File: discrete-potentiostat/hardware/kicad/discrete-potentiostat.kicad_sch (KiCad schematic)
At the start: 54 parts, among them J1 ELECTRODES, J2 SWD, U1 BQ51050BRHLR, U2 MIC5205-3.3YM5, U3 MDBT42Q-1MV2, U4 OPA2391, U5 REF35102QDBVR

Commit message: Replace BQ51050B direct-charge with BQ51013B + MCP73832 two-stage charging
Resolves the coin-cell charging risk: TI states BQ5105xB does not regulate
well below ~200mA, unsuitable for a 40mAh LIR2032. New chain follows TI's
guidance (Qi receiver -> 5V rail -> dedicated low-current charger), using
hand-solderable packages instead of the WCSP-only BQ51003/BQ25100 combo:

- BQ51013BRHLR: Qi WPC v1.2 receiver, regulated 5V out, VQFN-20. Pin map
  is the verified BQ51050BRHL family symbol with the two differing pins
  confirmed against the datasheet (4 OUT, 10 EN1). EN1=EN2=GND enables
  wireless; ILIM RILIM=250/IMAX -> 2.52k = 100mA; NTC stays on TS/CTRL.
- MCP73832T-2ACI/OT (official KiCad symbol): 4.2V linear charger,
  ICHG=1000/RPROG=20mA (0.5C), ~1.5mA termination, open-drain STAT ->
  CHG_N with the existing 100k pullup to 3V3.

Schematic regenerated and re-verified: all 38 design nets match the
kicad-cli extracted netlist exactly. Docs (README/design/BOM/firmware
plan/kicad README) updated to the two-stage chain; BQ51003+BQ25100 noted
as the drop-in denser alternative.

Co-Authored-By: Claude Fable 5 <noreply@anthropic.com>
Claude-Session: https://claude.ai/code/session_01GUNJUwfGKqvkZFmTaLQRu3
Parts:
- removed U1: BQ51050BRHLR, Package_DFN_QFN:Texas_VQFN-RHL-20, symbol Battery_Management:BQ51050BRHL
- added C27: 4.7u 10V, Capacitor_SMD:C_0603_1608Metric, symbol Device:C
- added U1: BQ51013BRHLR, Package_DFN_QFN:Texas_VQFN-RHL-20, symbol pstat:BQ51013BRHL
- added U6: MCP73832T-2ACI/OT, Package_TO_SOT_SMD:SOT-23-5, symbol Battery_Management:MCP73832-2-OT
- C10: value 1u 10V -> 4.7u 10V; footprint Capacitor_SMD:C_0402_1005Metric -> Capacitor_SMD:C_0603_1608Metric
- R1: value 15.4k 1% -> 2.32k 1%
- R3: value 2.4k 1% -> 49.9k 1%
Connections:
- net +BATT: now also C27.1, U6.3 (V_{BAT}); no longer C10.1, C11.1
- net AC1: now also U1.2 (AC1)
- net AC2: now also U1.19 (AC2)
- net BOOT1: now also U1.3 (BOOT1)
- net BOOT2: now also U1.17 (BOOT2)
- net CHG_N: now also U6.1 (STAT)
- net CLAMP1: now also U1.5 (CLAMP1)
- net CLAMP2: now also U1.16 (CLAMP2)
- net COMM1: now also U1.6 (COMM1)
- net COMM2: now also U1.15 (COMM2)
- net FOD: now also U1.14 (FOD)
- net GND: now also C27.2, U1.1 (PGND), U1.10 (EN1), U1.11 (EN2), U1.20 (PGND), U1.21 (PGND), U1.9 (AD), U6.2 (V_{SS})
- net ILIM: now also U1.12 (ILIM)
- net RECT: now also U1.18 (RECT)
- net TS: now also U1.13 (TS/CTRL)
- net TERM renamed PROG
- net PROG: now also U6.5 (PROG)
- new net V5OUT: C10.1, C11.1, U1.4 (OUT), U6.4 (V_{DD})
- no-connect marks 28 -> 29
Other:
- note added: "DISCRETE POTENTIOSTAT - wireless-charged 3-electrode chronoamperometry E_cell = WE - RE = 1.024V - 0.512V = +0.512V fixed. I_WE = (V(ADC_P)-V(ADC_N))/RF DESIGN NOTES / VERIFY BEFORE LAYOUT 1. CHARGING: two-stage per TI guidance for small cells. BQ51013B = Qi receiver with regulated 5V (V5OUT), ILIM: RILIM = 250/IMAX = R1+R2 = 2.52k -> IMAX 100mA (HW limit 120mA). MCP73832-2 (4.2V) charges the LIR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"
- note added: "QI RECEIVER 5V (BQ51013B) + 20mA CHARGER (MCP73832)"
- note removed: "DISCRETE POTENTIOSTAT - wireless-charged 3-electrode chronoamperometry E_cell = WE - RE = 1.024V - 0.512V = +0.512V fixed. I_WE = (V(ADC_P)-V(ADC_N))/RF DESIGN NOTES / VERIFY BEFORE LAYOUT 1. CHARGE CURRENT: IBULK = 314/RILIM = 314/(R1+R2) = 314/15.6k = 20mA (LIR2032 0.5C). TI states BQ5105xB regulates best >=200mA; at 20mA expect loose regulation and wide termination spread (R3 2.4k = 10% term).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"
- note removed: "QI WIRELESS RECEIVER + CHARGER (BQ51050B)"

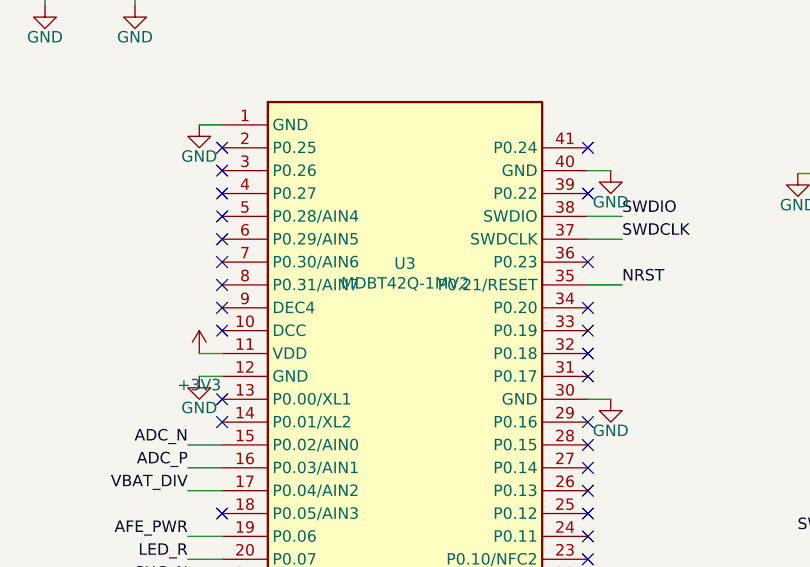
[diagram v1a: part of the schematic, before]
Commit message: Fix module part number: MDBT42Q-512KV2 (no 1MV2 variant exists for nRF52832)
Co-Authored-By: Claude Fable 5 <noreply@anthropic.com>
Claude-Session: https://claude.ai/code/session_01GUNJUwfGKqvkZFmTaLQRu3
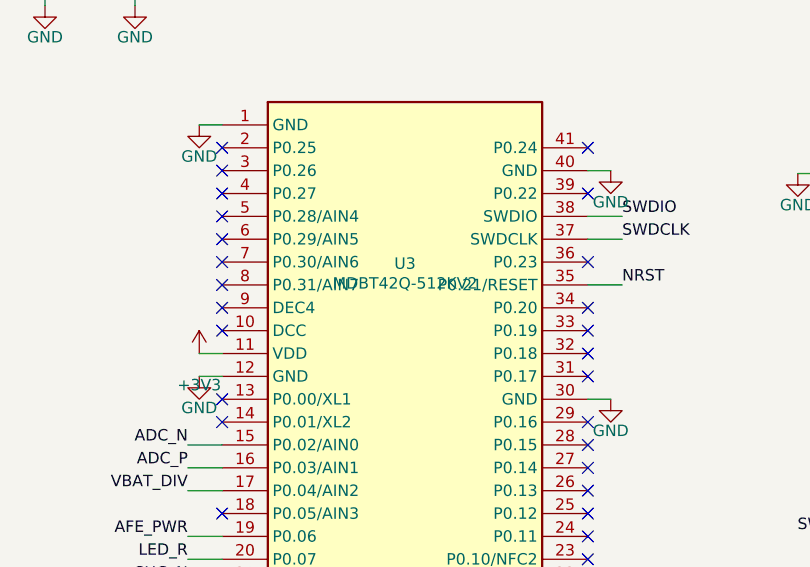
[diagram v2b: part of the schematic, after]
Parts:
- U3: value MDBT42Q-1MV2 -> MDBT42Q-512KV2

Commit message: Swap Qi coil to 760308101214 (19mm/26uH): smaller AND cheaper
The 26.3mm coil was a part-selection artifact, not a requirement — the
original sizing logic (device bounded by the battery) is restored. The
19mm WE-WPCC receiver coil costs less (~$7 vs ~$11), shrinks the PCB
from ~28mm to ~23mm disc, and our 0.13W charge load easily tolerates the
reduced coupling. Resonant caps retuned: C1 56n->100n, C2 560p->1n C0G.
Schematic regenerated, netlist re-verified (PASS); size/cost review
updated to the battery-bounded premise.

Co-Authored-By: Claude Fable 5 <noreply@anthropic.com>
Claude-Session: https://claude.ai/code/session_01GUNJUwfGKqvkZFmTaLQRu3
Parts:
- C1: value 56n C0G 50V -> 100n C0G 50V; footprint Capacitor_SMD:C_1206_3216Metric -> Capacitor_SMD:C_1210_3225Metric
- C2: value 560p C0G 50V -> 1n C0G 50V
- L1: value 760308101303 47uH -> 760308101214 26uH; footprint pstat:Wurth_760308101303 -> pstat:Wurth_760308101214

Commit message: Swap Qi coil to TDK WR202010-18M8-ID (20x20x1.0mm, 11uH, ~$3.6)
Cheapest verified candidate (half the 19mm Wurth) with the same footprint
class as the battery. Square outline: 22x22mm rounded-square puck instead
of a round disc (20x20 diagonal is 28.3mm). Resonant caps retuned for
11uH: C1 220nF C0G (fs 102kHz), C2 2.2nF C0G (fd ~1MHz). Schematic
regenerated, netlist verified (PASS).

Co-Authored-By: Claude Fable 5 <noreply@anthropic.com>
Claude-Session: https://claude.ai/code/session_01GUNJUwfGKqvkZFmTaLQRu3
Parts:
- C1: value 100n C0G 50V -> 220n C0G 50V
- C2: value 1n C0G 50V -> 2.2n C0G 50V
- L1: value 760308101214 26uH -> WR202010-18M8-ID 11uH; footprint pstat:Wurth_760308101214 -> pstat:TDK_WR202010

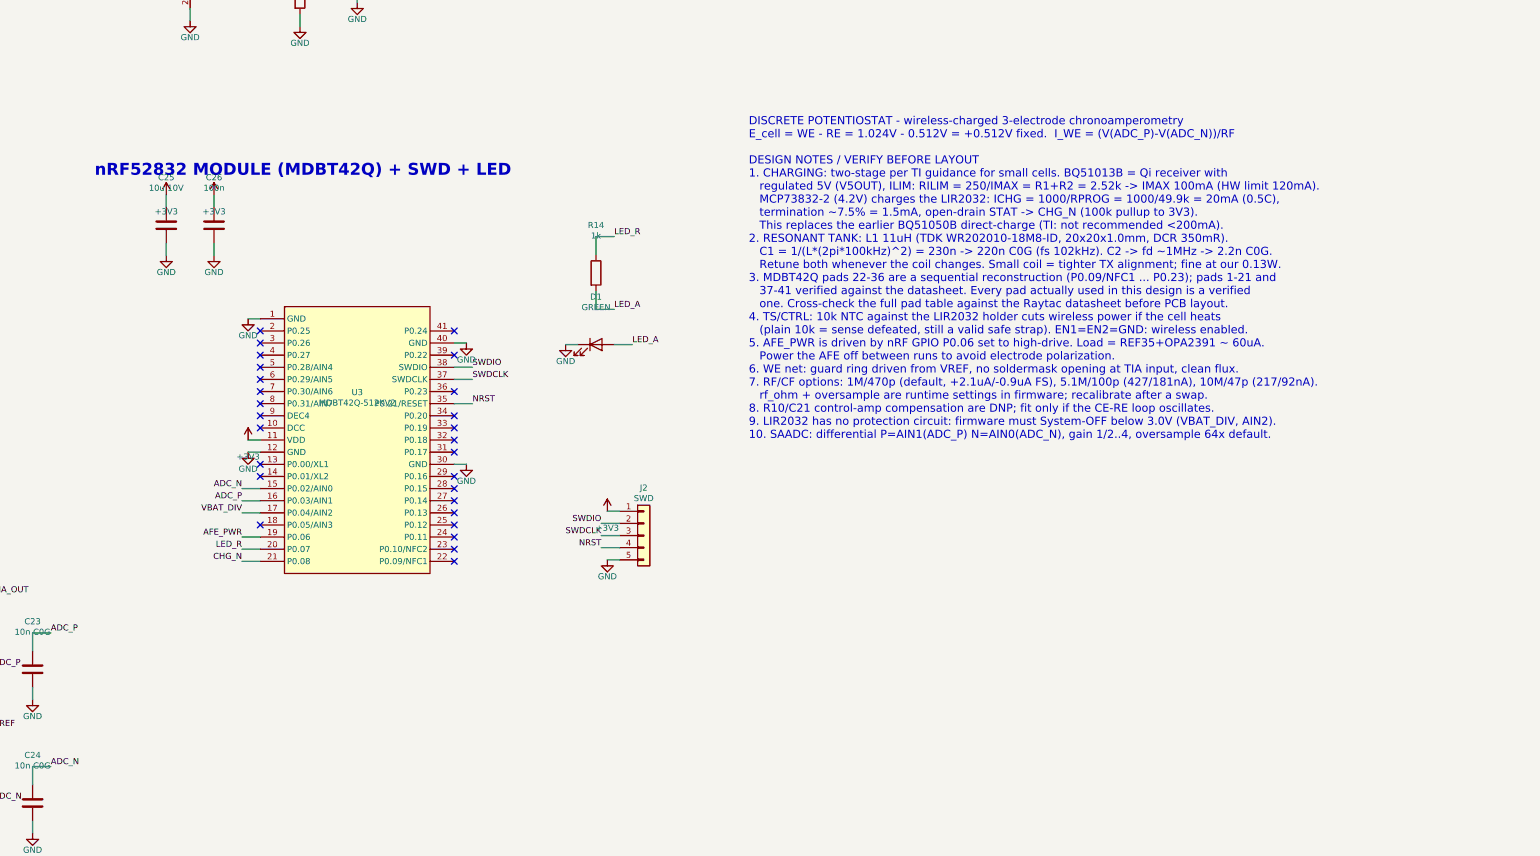
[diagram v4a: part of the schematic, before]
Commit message: Switch MCU to chip-down nRF52832-QFAA per user decision
Module certification inheritance is moot (intentional-radiator cert is
budgeted anyway), so the design drops MDBT42Q for the bare chip:

- nRF52832-QFAA on the verified official KiCad symbol (48+EP pin map)
- 32MHz crystal (CL 8pF) + 12pF loads; no 32k crystal -> LFRC synth
- RF front-end: Johanson 2450FM07A0029 (nRF52-QFN-specific matched LPF,
  replaces discrete LC guesswork) -> 0R/DNP tee tuning slots ->
  2450AT18B0100001E chip antenna
- Nordic QFN48 reference decoupling: DEC1 100n, DEC4 1u, DEC2/DEC3 NC,
  VDD 100n x3 + 4.7u bulk, DCC->DEC4 via 10uH+15nH (LDO-safe if unused)
- Same GPIO functions remapped to chip pins (AIN0/1/2 = 4/5/6, etc.)

Netlist re-verified: 47 design nets match kicad-cli extraction (PASS).
Docs updated; module-vs-chipdown.md records the decision and premise.

Co-Authored-By: Claude Fable 5 <noreply@anthropic.com>
Claude-Session: https://claude.ai/code/session_01GUNJUwfGKqvkZFmTaLQRu3
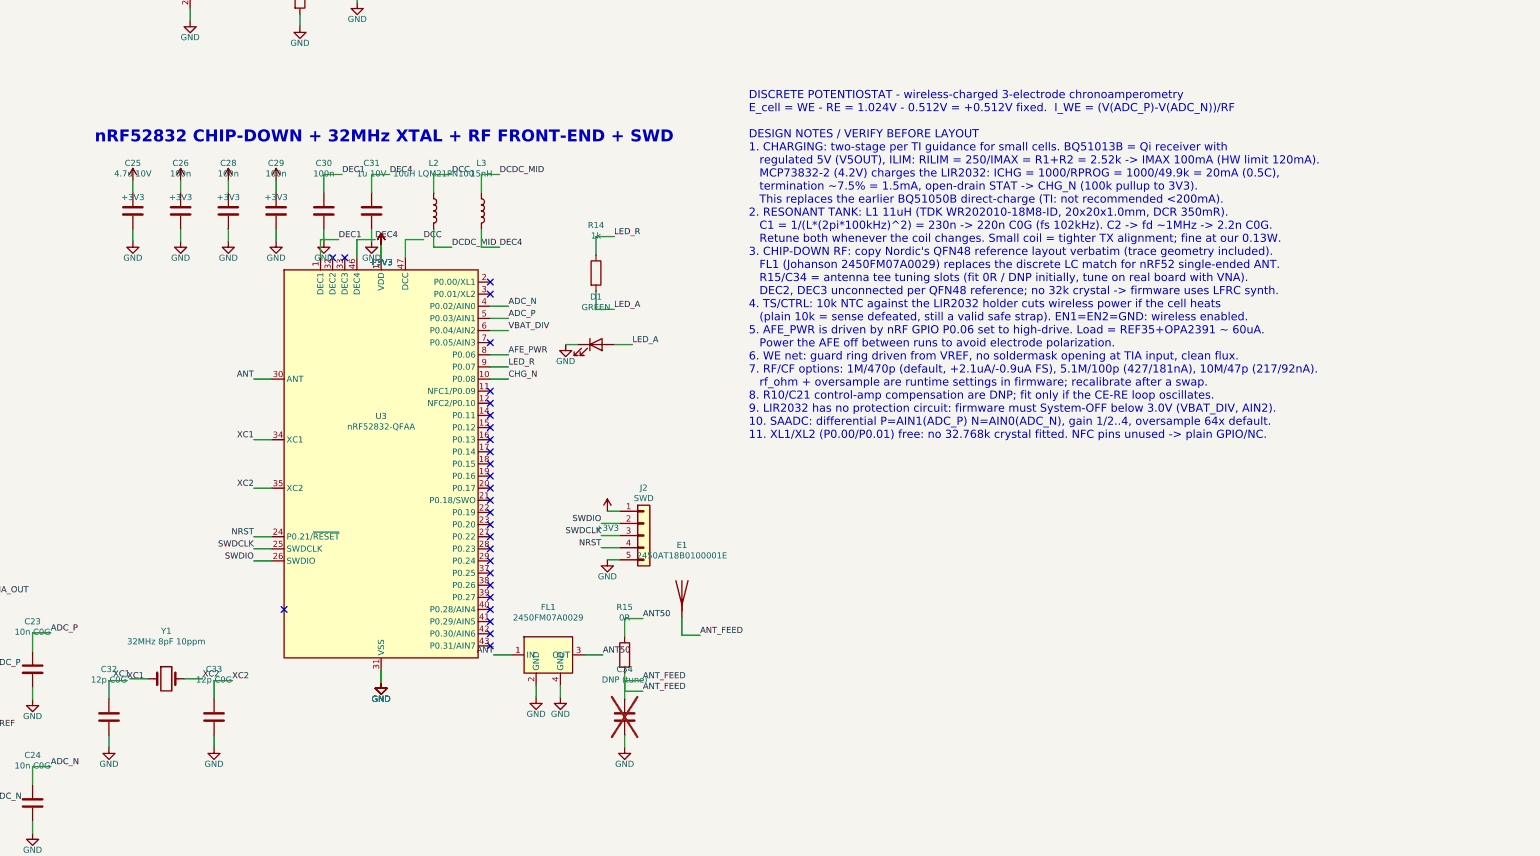
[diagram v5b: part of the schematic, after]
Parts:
- removed U3: MDBT42Q-512KV2, pstat:Raytac_MDBT42Q, symbol pstat:MDBT42Q
- added C28, C29, C30: 100n, Capacitor_SMD:C_0402_1005Metric, symbol Device:C
- added C31: 1u 10V, Capacitor_SMD:C_0402_1005Metric, symbol Device:C
- added C32, C33: 12p C0G, Capacitor_SMD:C_0402_1005Metric, symbol Device:C
- added C34: DNP (tune), Capacitor_SMD:C_0402_1005Metric, symbol Device:C
- added E1: 2450AT18B0100001E, pstat:Johanson_2450AT18B100, symbol Device:Antenna
- added FL1: 2450FM07A0029, pstat:Johanson_0402_4pin, symbol pstat:2450FM07A0029
- added L2: 10uH LQM21PN100, Inductor_SMD:L_0805_2012Metric, symbol Device:L
- added L3: 15nH, Inductor_SMD:L_0402_1005Metric, symbol Device:L
- added R15: 0R, Resistor_SMD:R_0402_1005Metric, symbol Device:R
- added U3: nRF52832-QFAA, Package_DFN_QFN:QFN-48-1EP_6x6mm_P0.4mm_EP4.6x4.6mm, symbol MCU_Nordic:nRF52832-QFxx
- added Y1: 32MHz 8pF 10ppm, Crystal:Crystal_SMD_3225-4Pin_3.2x2.5mm, symbol Device:Crystal
- C25: value 10u 10V -> 4.7u 10V
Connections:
- net +3V3: now also C28.1, C29.1, U3.13 (VDD), U3.36 (VDD), U3.48 (VDD)
- net ADC_N: now also U3.4 (P0.02/AIN0)
- net ADC_P: now also U3.5 (P0.03/AIN1)
- net AFE_PWR: now also U3.8 (P0.06)
- net CHG_N: now also U3.10 (P0.08)
- net GND: now also C28.2, C29.2, C30.2, C31.2, C32.2, C33.2, C34.2, FL1.2 (GND), FL1.4 (GND), U3.31 (VSS), U3.45 (VSS), U3.49 (VSS)
- net LED_R: now also U3.9 (P0.07)
- net NRST: now also U3.24 (P0.21/~{RESET})
- net SWDCLK: now also U3.25 (SWDCLK)
- net SWDIO: now also U3.26 (SWDIO)
- net VBAT_DIV: now also U3.6 (P0.04/AIN2)
- new net ANT: FL1.1 (IN), U3.30 (ANT)
- new net ANT50: FL1.3 (OUT), R15.1
- new net ANT_FEED: C34.1, E1.1 (A), R15.2
- new net DCC: L2.1, U3.47 (DCC)
- new net DCDC_MID: L2.2, L3.1
- new net DEC1: C30.1, U3.1 (DEC1)
- new net DEC4: C31.1, L3.2, U3.46 (DEC4)
- new net XC1: C32.1, U3.34 (XC1), Y1.1
- new net XC2: C33.1, U3.35 (XC2), Y1.2
- no-connect marks 29 -> 30
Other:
- note added: "nRF52832 CHIP-DOWN + 32MHz XTAL + RF FRONT-END + SWD"
- note removed: "nRF52832 MODULE (MDBT42Q) + SWD + LED"
